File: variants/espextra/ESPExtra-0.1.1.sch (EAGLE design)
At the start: 12 parts, among them U1 ESP12E_DEVKIT, U2 MCP23S17SP, U3 MCP23S17SP, U4 MCP3008

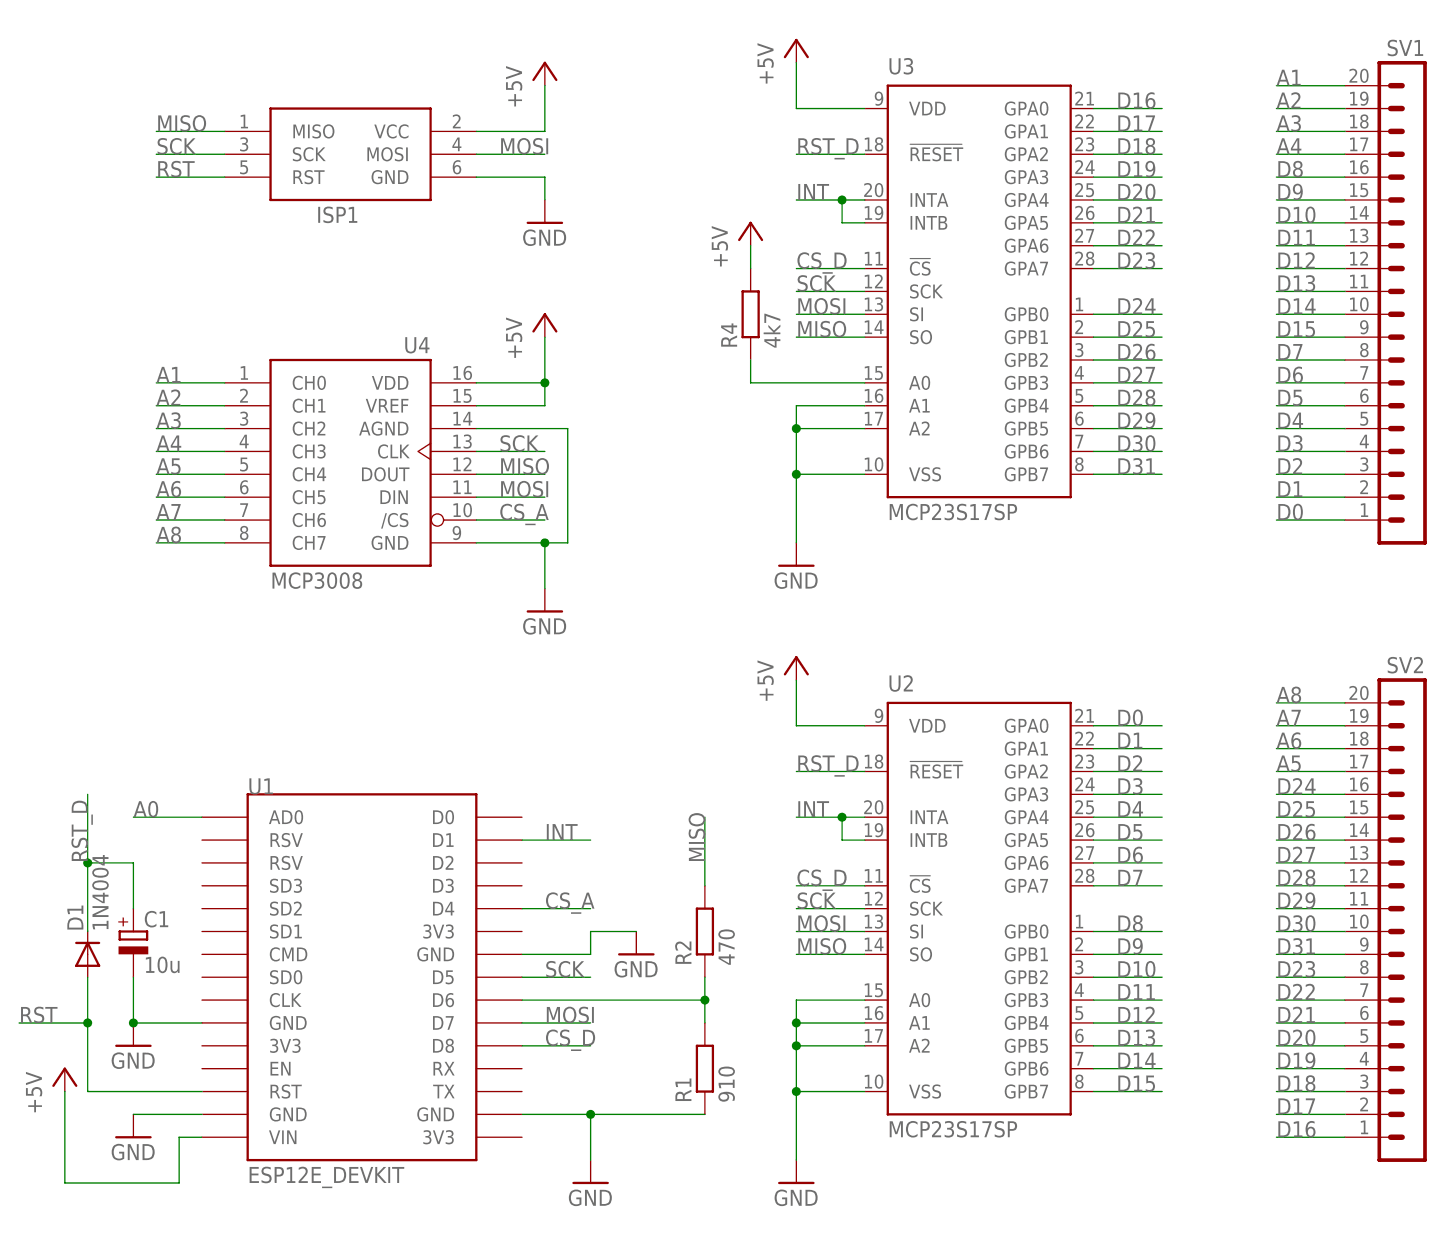
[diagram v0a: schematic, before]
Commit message: Updated the board schematic to use 3V3. Using 5V is not working.
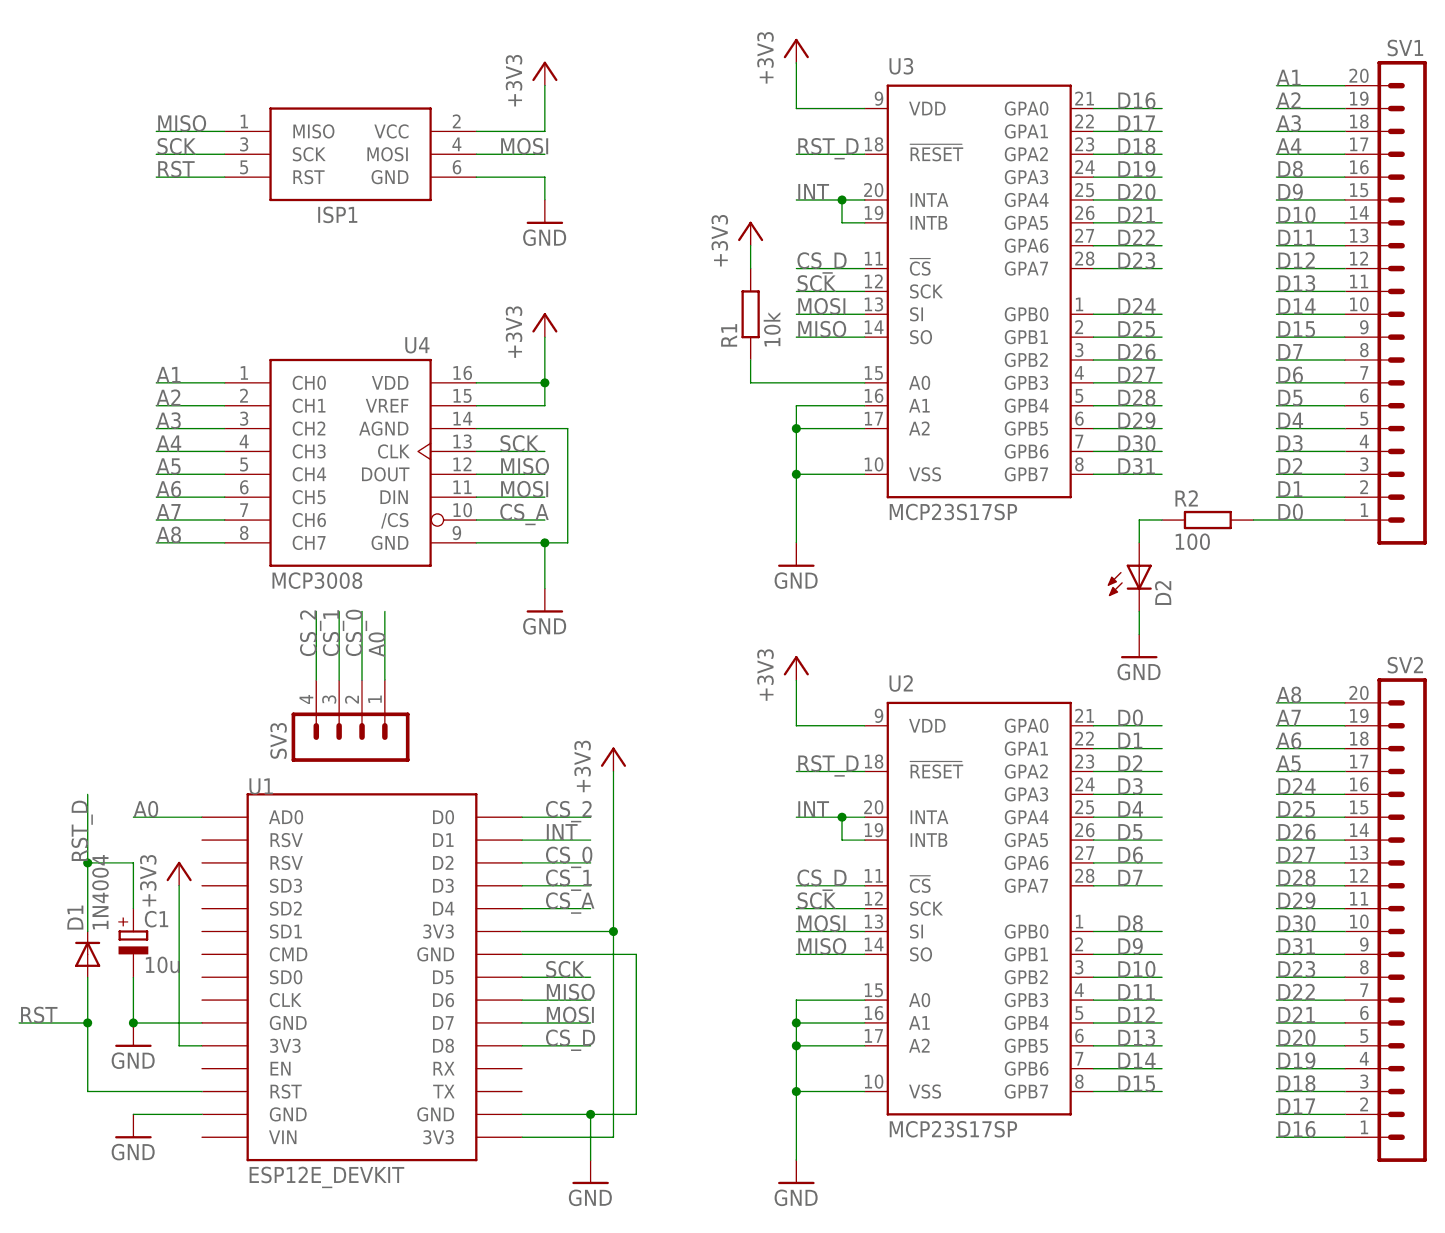
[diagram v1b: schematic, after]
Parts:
- removed R4: 4k7, resistor:R-EU_0204/5
- added D2: (no value), led:LED3MM
- added SV3: (no value), con-lstb:MA04-1
- R1: value 910 -> 10k
- R2: value 470 -> 100
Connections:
- removed net +5V: ISP1.VCC, R4.2, U1.VIN, U2.VDD, U3.VDD, U4.VDD, U4.VREF
- removed net N$11: R1.2, R2.1, U1.D6
- new net +3V3: ISP1.VCC, R1.2, U1.3V3@0, U1.3V3@1, U1.3V3@2, U2.VDD, U3.VDD, U4.VDD, U4.VREF
- new net CS_0: SV3.2, U1.D2
- new net CS_1: SV3.3, U1.D3
- new net CS_2: SV3.4, U1.D0
- new net N$1: D2.A, R2.1
- net A0: now also SV3.1
- net D0: now also R2.2
- net GND: now also D2.C; no longer R1.1
- net MISO: now also U1.D6; no longer R2.2
- net N$25: now also R1.1; no longer R4.1
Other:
- moved on the sheet: R1, R2
